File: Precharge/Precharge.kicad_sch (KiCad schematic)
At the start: 66 parts, among them J1 Conn_01x02, J2 Conn_01x02, J3 Molex MicroFit, J4 Conn_02x03_Counter_Clockwise, K1 KT12-1A-40L-THT, Q1 AO3400A, Q2 AO3400A, Q3 AO3400A, U1 LM393, U2 4N35, U3 4N35

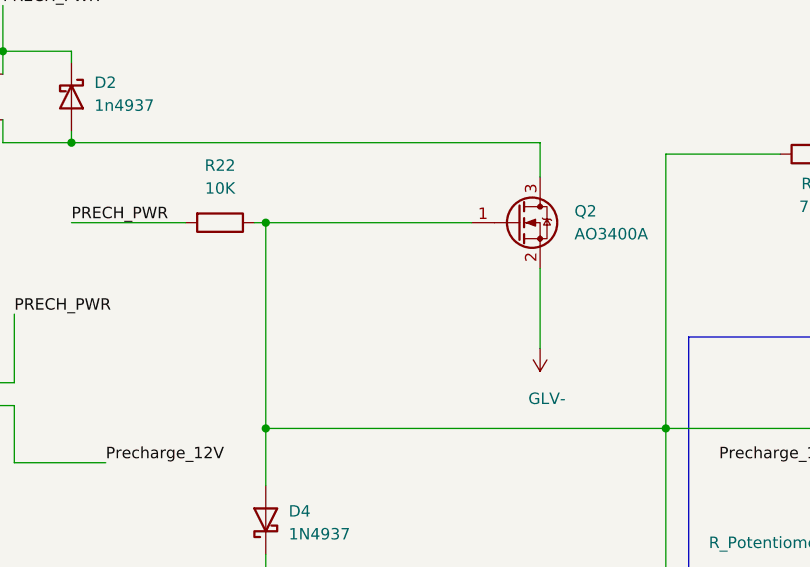
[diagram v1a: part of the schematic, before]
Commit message: Modify TSAL PCB and use relative paths for libraries
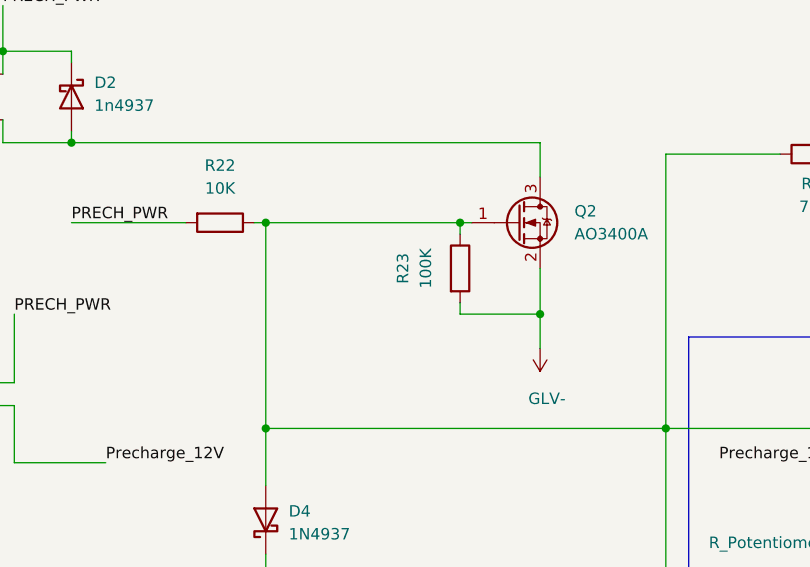
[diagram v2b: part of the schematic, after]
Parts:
- added R23: 100K, Resistor_SMD:R_0603_1608Metric_Pad0.98x0.95mm_HandSolder, symbol Device:R
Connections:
- net GLV-: now also R23.2
- net at D4.2 (A), D5.1 (K), Q2.1 (G)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: now also R23.1
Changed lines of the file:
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@@
+	)
+	(junction
+		(at 251.46 74.93)
+		(diameter 0)
+		(color 0 0 0 0)
 	)
 	(junction
@@
 	)
 	(junction
+		(at 260.35 85.09)
+		(diameter 0)
+		(color 0 0 0 0)
+	)
+	(junction
 		(at 317.5 109.22)
 		(diameter 0)
@@
 	(wire
 		(pts
-			(xy 260.35 80.01) (xy 260.35 88.9)
+			(xy 260.35 80.01) (xy 260.35 85.09)
 		)
 		(stroke
@@
 		(pts
 			(xy 198.12 124.46) (xy 201.93 124.46)
+		)
+		(stroke
+			(width 0)
+			(type default)
+		)
+	)
+	(wire
+		(pts
+			(xy 260.35 85.09) (xy 260.35 88.9)
 		)
 		(stroke
@@
 	(wire
 		(pts
+			(xy 251.46 76.2) (xy 251.46 74.93)
+		)
+		(stroke
+			(width 0)
+			(type default)
+		)
+	)
+	(wire
+		(pts
 			(xy 236.22 210.82) (xy 232.41 210.82)
 		)
@@
 	(wire
 		(pts
+			(xy 251.46 74.93) (xy 252.73 74.93)
+		)
+		(stroke
+			(width 0)
+			(type default)
+		)
+	)
+	(wire
+		(pts
 			(xy 273.05 210.82) (xy 274.32 210.82)
 		)
@@
 	(wire
 		(pts
+			(xy 251.46 85.09) (xy 260.35 85.09)
+		)
+		(stroke
+			(width 0)
+			(type default)
+		)
+	)
+	(wire
+		(pts
 			(xy 97.79 168.91) (xy 97.79 171.45)
 		)
@@
 	(wire
 		(pts
-			(xy 229.87 74.93) (xy 252.73 74.93)
+			(xy 229.87 74.93) (xy 251.46 74.93)
 		)
 		(stroke
@@
 		(pts
 			(xy 81.28 124.46) (xy 85.09 124.46)
+		)
+		(stroke
+			(width 0)
+			(type default)
+		)
+	)
+	(wire
+		(pts
+			(xy 251.46 83.82) (xy 251.46 85.09)
 		)
 		(stroke
@@
 					(unit 1)
 				)
+			)
+		)
+	)
+	(symbol
+		(lib_id "Device:R")
+		(at 251.46 80.01 0)
+		(unit 1)
+		(exclude_from_sim no)
+		(in_bom yes)
+		(on_board yes)
+		(dnp no)
+		(property "Reference" "R23"
+			(at 245.11 80.01 90)
+			(effects
+				(font
+					(size 1.27 1.27)
+				)
+			)
+		)
+		(property "Value" "100K"
+			(at 247.65 80.01 90)
+			(effects
+				(font
+					(size 1.27 1.27)
+				)
+			)
+		)
+		(property "Footprint" "Resistor_SMD:R_0603_1608Metric_Pad0.98x0.95mm_HandSolder"
+			(at 249.682 80.01 90)
+			(effects
+				(font
+					(size 1.27 1.27)
+				)
+				(hide yes)
+			)
+		)
+		(property "Datasheet" "~"
+			(at 251.46 80.01 0)
+			(effects
+				(font
+					(size 1.27 1.27)
+				)
+				(hide yes)
+			)
+		)
+		(property "Description" "Resistor"
+			(at 251.46 80.01 0)
+			(effects
+				(font
+					(size 1.27 1.27)
+				)
+				(hide yes)
+			)
+		)
+		(pin "2"
+		)
+		(pin "1"
+		)
+		(instances
+			(project "Precharge"
+				(path "/5679ed2e-bac1-400d-bcc5-1297256104b1"
+					(reference "R23")
+					(unit 1)
+				)

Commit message: minor changes
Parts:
- added R39: 10K, Resistor_SMD:R_0603_1608Metric_Pad0.98x0.95mm_HandSolder, symbol Device:R
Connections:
- net GLV-: now also R39.2
- net Precharge_12V: now also R39.1
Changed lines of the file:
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@@
 	(title_block
 		(title "Precharge Circuit")
-		(date "2024-11-01")
-		(rev "3.2")
+		(date "2025-01-10")
+		(rev "3.3")
 		(company "Formula Barton Racing")
 		(comment 1 "evanscesil@gmail.com")
@@
 	)
 	(junction
+		(at 201.93 95.25)
+		(diameter 0)
+		(color 0 0 0 0)
+	)
+	(junction
 		(at 373.38 210.82)
 		(diameter 0)
@@
 	(wire
 		(pts
-			(xy 201.93 101.6) (xy 212.09 101.6)
+			(xy 201.93 95.25) (xy 210.82 95.25)
 		)
 		(stroke
@@
 	(wire
 		(pts
+			(xy 201.93 95.25) (xy 201.93 97.79)
+		)
+		(stroke
+			(width 0)
+			(type default)
+		)
+	)
+	(wire
+		(pts
 			(xy 166.37 109.22) (xy 166.37 113.03)
 		)
@@
 	(wire
 		(pts
-			(xy 201.93 101.6) (xy 201.93 95.25)
-		)
-		(stroke
-			(width 0)
-			(type default)
-		)
-	)
-	(wire
-		(pts
 			(xy 124.46 92.71) (xy 124.46 102.87)
 		)
@@
 	)
 	(label "Precharge_12V"
-		(at 212.09 101.6 0)
+		(at 210.82 95.25 0)
 		(fields_autoplaced yes)
 		(effects
@@
 	)
 	(symbol
+		(lib_id "Device:R")
+		(at 201.93 101.6 0)
+		(unit 1)
+		(exclude_from_sim no)
+		(in_bom yes)
+		(on_board yes)
+		(dnp no)
+		(property "Reference" "R39"
+			(at 205.74 101.092 0)
+			(effects
+				(font
+					(size 1.27 1.27)
+				)
+			)
+		)
+		(property "Value" "10K"
+			(at 205.994 103.124 0)
+			(effects
+				(font
+					(size 1.27 1.27)
+				)
+			)
+		)
+		(property "Footprint" "Resistor_SMD:R_0603_1608Metric_Pad0.98x0.95mm_HandSolder"
+			(at 200.152 101.6 90)
+			(effects
+				(font
+					(size 1.27 1.27)
+				)
+				(hide yes)
+			)
+		)
+		(property "Datasheet" "~"
+			(at 201.93 101.6 0)
+			(effects
+				(font
+					(size 1.27 1.27)
+				)
+				(hide yes)
+			)
+		)
+		(property "Description" "Resistor"
+			(at 201.93 101.6 0)
+			(effects
+				(font
+					(size 1.27 1.27)
+				)
+				(hide yes)
+			)
+		)
+		(pin "2"
+		)
+		(pin "1"
+		)
+		(instances
+			(project "Precharge"
+				(path "/5679ed2e-bac1-400d-bcc5-1297256104b1"
+					(reference "R39")
+					(unit 1)
+				)
+			)
+		)
+	)
+	(symbol
 		(lib_id "Diode:1N5819")
 		(at 151.13 85.09 90)
@@
 					(unit 1)
 				)
+			)
+		)
+	)
+	(symbol
+		(lib_id "power:+12V")
+		(at 201.93 105.41 0)
+		(mirror x)
+		(unit 1)
+		(exclude_from_sim no)
+		(in_bom yes)
+		(on_board yes)
+		(dnp no)
+		(property "Reference" "#PWR010"
+			(at 201.93 101.6 0)
+			(effects
+				(font
+					(size 1.27 1.27)
+				)
+				(hide yes)
+			)
+		)
+		(property "Value" "GLV-"
+			(at 199.644 109.474 0)
+			(effects
+				(font
+					(size 1.27 1.27)
+				)
+				(justify left)
+			)
+		)
+		(property "Footprint" ""
+			(at 201.93 105.41 0)
+			(effects
+				(font
+					(size 1.27 1.27)
+				)
+				(hide yes)
+			)
+		)
+		(property "Datasheet" ""
+			(at 201.93 105.41 0)
+			(effects
+				(font
+					(size 1.27 1.27)
+				)
+				(hide yes)
+			)
+		)
+		(property "Description" ""
+			(at 201.93 105.41 0)
+			(effects
+				(font
+					(size 1.27 1.27)
+				)
+				(hide yes)
+			)
+		)
+		(pin "1"
+		)
+		(instances
+			(project "Precharge"
+				(path "/5679ed2e-bac1-400d-bcc5-1297256104b1"
+					(reference "#PWR010")
+					(unit 1)
+				)

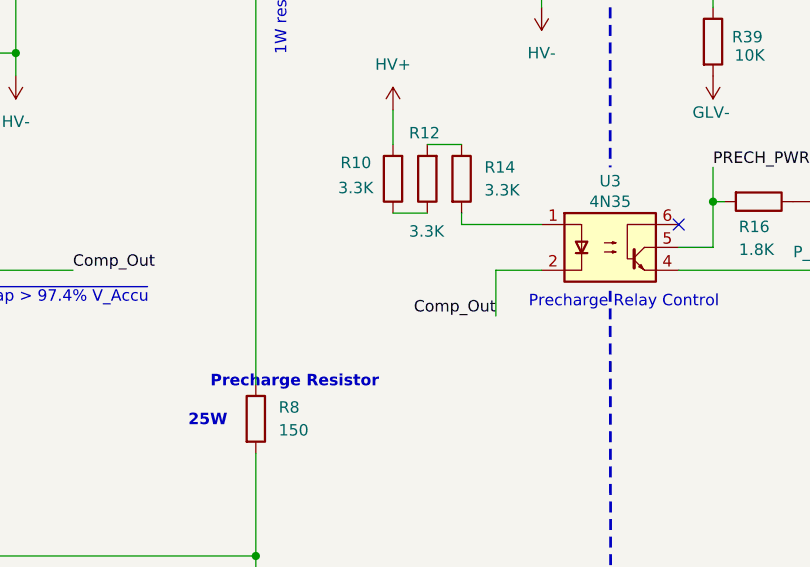
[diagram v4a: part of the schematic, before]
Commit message: Increase width of SDC track
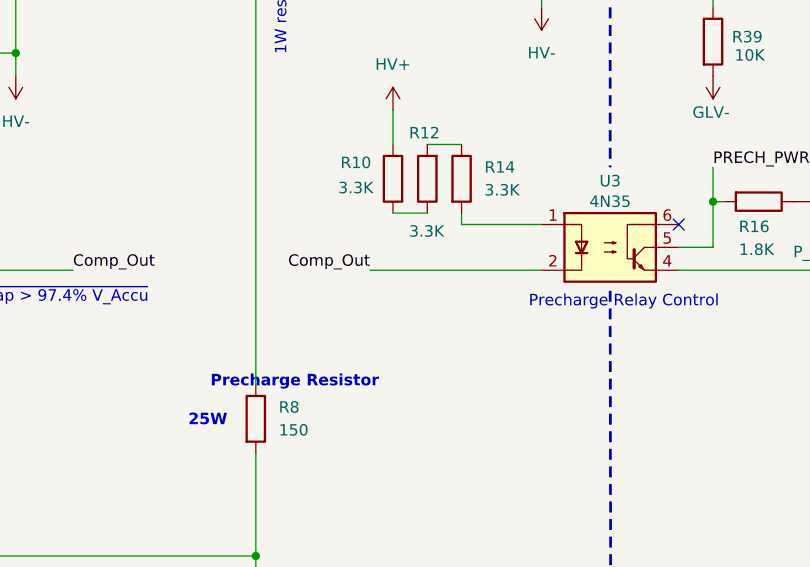
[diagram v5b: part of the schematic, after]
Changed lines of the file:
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@@
 	(wire
 		(pts
-			(xy 177.8 127) (xy 182.88 127)
+			(xy 163.83 127) (xy 182.88 127)
 		)
 		(stroke
@@
 	(wire
 		(pts
-			(xy 177.8 132.08) (xy 177.8 127)
-		)
-		(stroke
-			(width 0)
-			(type default)
-		)
-	)
-	(wire
-		(pts
 			(xy 238.76 260.35) (xy 240.03 260.35)
 		)
@@
 	)
 	(label "Comp_Out"
-		(at 177.8 132.08 180)
-		(effects
-			(font
+		(at 163.83 127 180)
+		(effects
+			(font

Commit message: Precharge modifications
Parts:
- removed R20, R23: 100K, Resistor_SMD:R_0603_1608Metric_Pad0.98x0.95mm_HandSolder, symbol Device:R
- added TP6: TestPoint, Connector_Pin:Pin_D1.0mm_L10.0mm, symbol Connector:TestPoint
- added TP7: GLV-, Connector_Pin:Pin_D1.0mm_L10.0mm, symbol Connector:TestPoint
- D6: now not fitted
- Q1: value AO3400A -> CJ2310
- R33, R34, R35, R36, R37, R38: value 10K -> 8.6K
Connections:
- net GLV-: now also TP7.1; no longer J3.1 (Pin_1)
- net HV-: now also TP6.1
- net PRECH_PWR: no longer D2.1 (K), K1.COIL2, R16.2, R17.1, R19.1, R26.1, R28.1, R30.1, R32.1, U2.5, U3.5
- net AIR+_Con renamed AIR+_GND
- new net GLV+: D2.1 (K), J3.1 (Pin_1), K1.COIL2, R16.2, R17.1, R19.1, R26.1, R28.1, R30.1, R32.1, U2.5, U3.5
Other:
- note added: "AIR+_GND is the "negative" lead of AIR+. 12V when SDC is present. Short to GND to activate AIR. PRECH_PWR is the SDC supply and the positive lead of the AIR"
- note added: "AIR+_Out and AIR-_Out are the aux contacts"
- note removed: "AIR+_Con is the "negative" lead of AIR+. 12V when SDC is present. Short to GND to activate AIR."
- moved on the sheet: J3, Q1, R15, R17, R24, R28, R29, R30, R35, R36, R38, TP2
